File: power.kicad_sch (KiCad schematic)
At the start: 0 parts

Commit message: Fixed actuator channels to make GPIO expander sink instead of source current
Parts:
- added K?: J115F11C, actuation:J115F11C, symbol actuation:J115F11C
- added U?: TLI4971, Package_SON:Infineon_PG-TISON-8-5, symbol actuation:TLI4971
- added U?: ADS1110, Package_TO_SOT_SMD:SOT-23-6, symbol Analog_ADC:ADS1110
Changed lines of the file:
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@@
 (kicad_sch (version 20211123) (generator eeschema)
   (paper "A4")
+  (symbol (lib_id "actuation:J115F11C") (at 80.01 67.31 0) (unit 1)
+    (in_bom yes) (on_board yes) (fields_autoplaced)
+    (property "Reference" "K?" (id 0) (at 80.01 54.61 0))
+    (property "Value" "J115F11C" (id 1) (at 80.01 57.15 0))
+    (property "Footprint" "actuation:J115F11C" (id 2) (at 80.01 76.2 0)
+      (effects (font (size 1.27 1.27)) hide)
+    )
+    (property "Datasheet" "https://www.citrelay.com/Catalog%20Pages/RelayCatalog/J115F%2050amp.pdf" (id 3) (at 80.01 78.74 0)
+      (effects (font (size 1.27 1.27)) hide)
+    )
+    (property "MPN" "J115F11CH12VDCSH1.5U" (id 4) (at 80.01 81.28 0)
+      (effects (font (size 1.27 1.27)) hide)
+    )
+    (pin "1")
+    (pin "2")
+    (pin "3")
+    (pin "4")
+    (pin "5")
+  )
+  (symbol (lib_id "actuation:TLI4971") (at 124.46 90.17 0) (unit 1)
+    (in_bom yes) (on_board yes) (fields_autoplaced)
+    (property "Reference" "U?" (id 0) (at 124.46 85.09 0))
+    (property "Value" "TLI4971" (id 1) (at 124.46 87.63 0))
+    (property "Footprint" "Package_SON:Infineon_PG-TISON-8-5" (id 2) (at 124.46 109.22 0)
+      (effects (font (size 1.27 1.27)) hide)
+    )
+    (property "Datasheet" "https://www.infineon.com/dgdl/Infineon-TLI4971_25_50_75_120-DataSheet-v01_20-EN.pdf" (id 3) (at 124.46 111.76 0)
+      (effects (font (size 1.27 1.27)) hide)
+    )
+    (property "MPN" "TLI4971A050T5UE0001XUMA1" (id 4) (at 124.46 114.3 0)
+      (effects (font (size 1.27 1.27)) hide)
+    )
+    (pin "1")
+    (pin "2")
+    (pin "3")
+    (pin "4")
+    (pin "5")
+    (pin "6")
+    (pin "7")
+    (pin "8")
+  )
+  (symbol (lib_id "Analog_ADC:ADS1110") (at 179.07 69.85 0) (unit 1)
+    (in_bom yes) (on_board yes) (fields_autoplaced)
+    (property "Reference" "U?" (id 0) (at 181.0894 57.15 0)
+      (effects (font (size 1.27 1.27)) (justify left))
+    )
+    (property "Value" "ADS1110" (id 1) (at 181.0894 59.69 0)
+      (effects (font (size 1.27 1.27)) (justify left))
+    )
+    (property "Footprint" "Package_TO_SOT_SMD:SOT-23-6" (id 2) (at 190.5 60.96 0)
+      (effects (font (size 1.27 1.27)) (justify left) hide)
+    )
+    (property "Datasheet" "http://www.ti.com/lit/ds/symlink/ads1110.pdf" (id 3) (at 171.45 60.96 0)
+      (effects (font (size 1.27 1.27)) hide)
+    )
+    (pin "1")
+    (pin "2")
+    (pin "3")
+    (pin "4")
+    (pin "5")
+    (pin "6")
+  )
 )

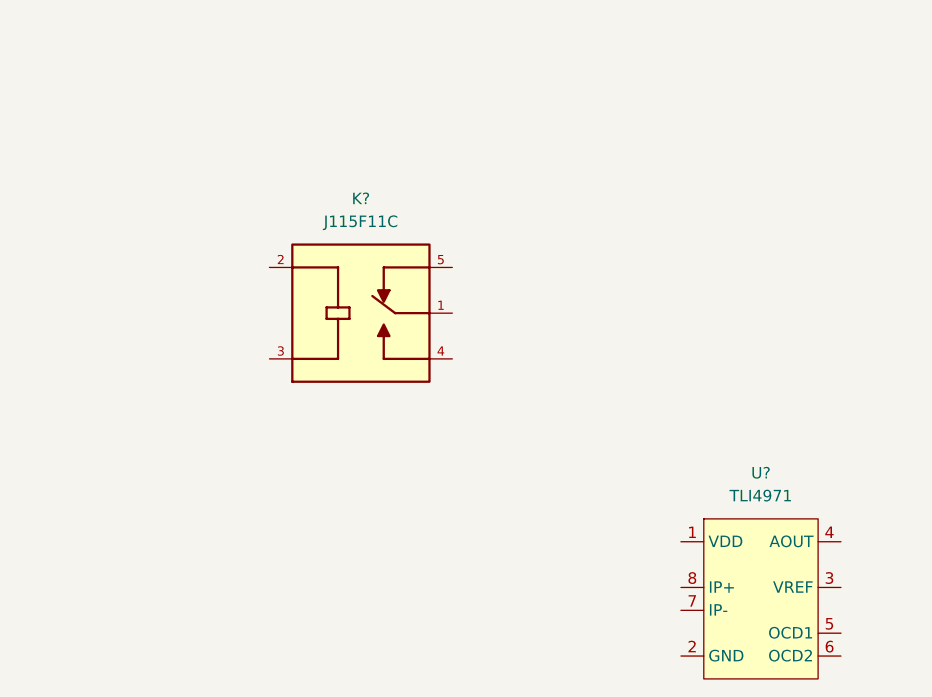
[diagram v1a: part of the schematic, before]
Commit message: Check-safe channel with buffer
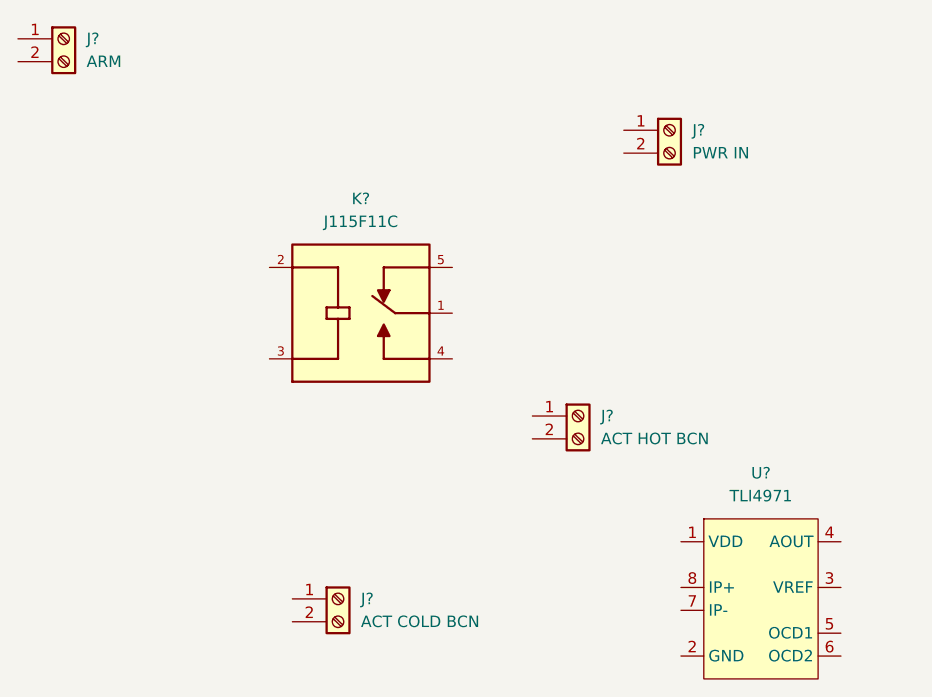
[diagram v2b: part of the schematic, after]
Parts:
- added J?: PWR IN, symbol Connector:Screw_Terminal_01x02
- added J?: ACT HOT BCN, symbol Connector:Screw_Terminal_01x02
- added J?: ACT COLD BCN, symbol Connector:Screw_Terminal_01x02
- added J?: ARM, symbol Connector:Screw_Terminal_01x02
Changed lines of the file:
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@@
     (pin "5")
+  )
+  (symbol (lib_id "Connector:Screw_Terminal_01x02") (at 114.3 46.99 0) (unit 1)
+    (in_bom yes) (on_board yes) (fields_autoplaced)
+    (property "Reference" "J?" (id 0) (at 116.84 46.9899 0)
+      (effects (font (size 1.27 1.27)) (justify left))
+    )
+    (property "Value" "PWR IN" (id 1) (at 116.84 49.5299 0)
+      (effects (font (size 1.27 1.27)) (justify left))
+    )
+    (property "Footprint" "" (id 2) (at 114.3 46.99 0)
+      (effects (font (size 1.27 1.27)) hide)
+    )
+    (property "Datasheet" "~" (id 3) (at 114.3 46.99 0)
+      (effects (font (size 1.27 1.27)) hide)
+    )
+    (pin "1")
+    (pin "2")
   )
   (symbol (lib_id "actuation:TLI4971") (at 124.46 90.17 0) (unit 1)
@@
     (pin "6")
   )
+  (symbol (lib_id "Connector:Screw_Terminal_01x02") (at 104.14 78.74 0) (unit 1)
+    (in_bom yes) (on_board yes) (fields_autoplaced)
+    (property "Reference" "J?" (id 0) (at 106.68 78.7399 0)
+      (effects (font (size 1.27 1.27)) (justify left))
+    )
+    (property "Value" "ACT HOT BCN" (id 1) (at 106.68 81.2799 0)
+      (effects (font (size 1.27 1.27)) (justify left))
+    )
+    (property "Footprint" "" (id 2) (at 104.14 78.74 0)
+      (effects (font (size 1.27 1.27)) hide)
+    )
+    (property "Datasheet" "~" (id 3) (at 104.14 78.74 0)
+      (effects (font (size 1.27 1.27)) hide)
+    )
+    (pin "1")
+    (pin "2")
+  )
+  (symbol (lib_id "Connector:Screw_Terminal_01x02") (at 77.47 99.06 0) (unit 1)
+    (in_bom yes) (on_board yes) (fields_autoplaced)
+    (property "Reference" "J?" (id 0) (at 80.01 99.0599 0)
+      (effects (font (size 1.27 1.27)) (justify left))
+    )
+    (property "Value" "ACT COLD BCN" (id 1) (at 80.01 101.5999 0)
+      (effects (font (size 1.27 1.27)) (justify left))
+    )
+    (property "Footprint" "" (id 2) (at 77.47 99.06 0)
+      (effects (font (size 1.27 1.27)) hide)
+    )
+    (property "Datasheet" "~" (id 3) (at 77.47 99.06 0)
+      (effects (font (size 1.27 1.27)) hide)
+    )
+    (pin "1")
+    (pin "2")
+  )
+  (symbol (lib_id "Connector:Screw_Terminal_01x02") (at 46.99 36.83 0) (unit 1)
+    (in_bom yes) (on_board yes) (fields_autoplaced)
+    (property "Reference" "J?" (id 0) (at 49.53 36.8299 0)
+      (effects (font (size 1.27 1.27)) (justify left))
+    )
+    (property "Value" "ARM" (id 1) (at 49.53 39.3699 0)
+      (effects (font (size 1.27 1.27)) (justify left))
+    )
+    (property "Footprint" "" (id 2) (at 46.99 36.83 0)
+      (effects (font (size 1.27 1.27)) hide)
+    )
+    (property "Datasheet" "~" (id 3) (at 46.99 36.83 0)
+      (effects (font (size 1.27 1.27)) hide)
+    )
+    (pin "1")
+    (pin "2")
+  )
 )

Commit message: Preliminary power scheme
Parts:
- J?: value ACT HOT BCN -> ACT HOT
- J?: value ACT COLD BCN -> ACT COLD
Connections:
- net VBUS: now reaches K?.1
- net VBUS: now also U?.7 (IP-)
- net at K?.2: now also J?.2 (Pin_2)
- net at K?.3: now also J?.1 (Pin_1)
- net Vdrive: now reaches K?.4
- net Vdrive: now also J?.1 (Pin_1)
- net VSAFE: now reaches K?.5
- net VSAFE: now also J?.1 (Pin_1)
- net at J?.1 (Pin_1): now also U?.8 (IP+)
- net GNDPWR: now reaches J?.2 (Pin_2)
- net GNDPWR: now also J?.2 (Pin_2), J?.2 (Pin_2)
- net +3.3V: now reaches U?.1 (VDD)
- net +3.3V: now also U?.5 (VDD)
- net GND: now reaches U?.2 (GND)
- net GND: now also U?.2 (GND)
- net at U?.3 (VREF): now also U?.6 (VIN-)
- net at U?.4 (AOUT): now also U?.1 (VIN+)
- net SCL: now reaches U?.3 (SCL)
- net SDA: now reaches U?.4 (SDA)
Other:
- moved on the sheet: J?, K?, U?

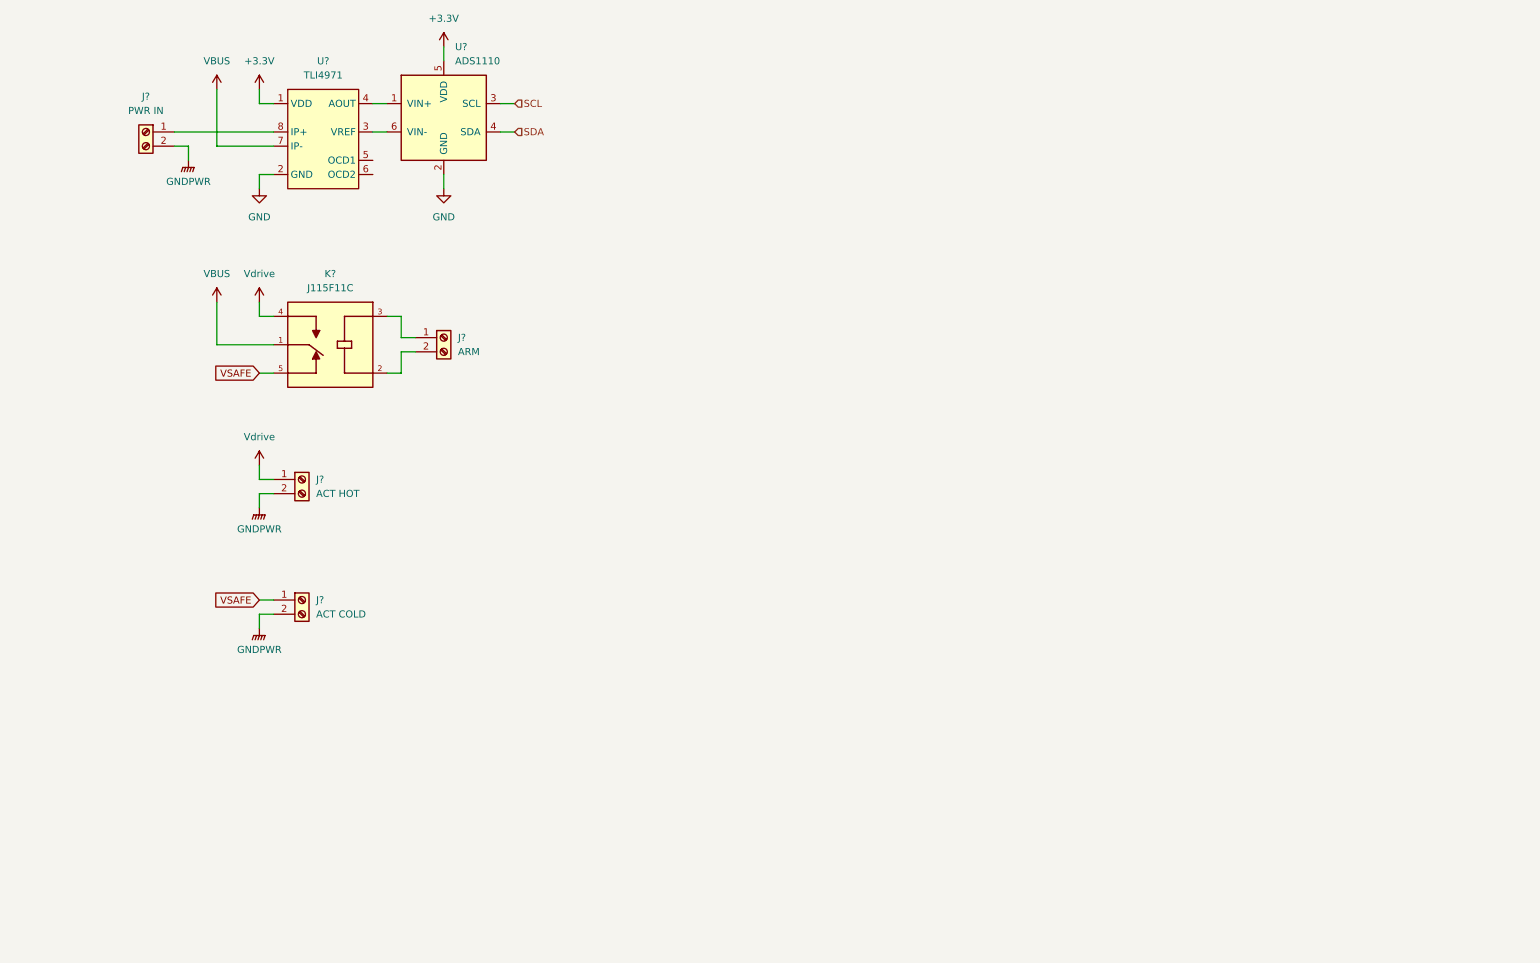
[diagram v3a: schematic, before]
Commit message: ADC filtering and decoupling for current sense
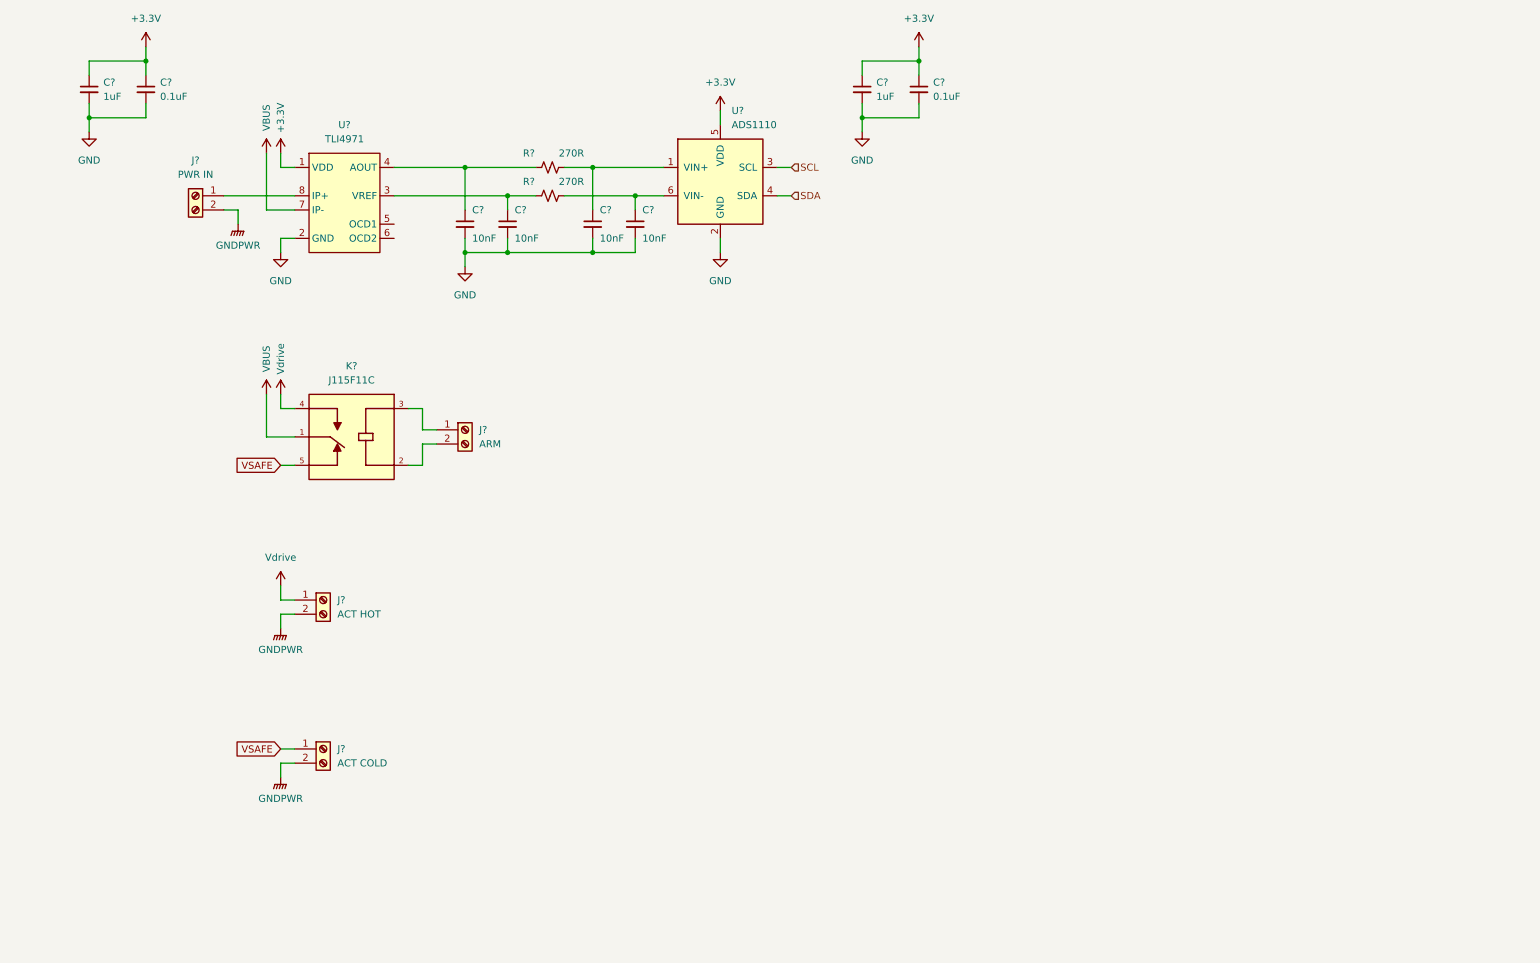
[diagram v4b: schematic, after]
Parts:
- added C? (x4): 10nF, symbol Device:C_Small
- added C? (x2): 1uF, Capacitor_SMD:C_0603_1608Metric, symbol Device:C_Small
- added C? (x2): 0.1uF, Capacitor_SMD:C_0603_1608Metric, symbol Device:C_Small
- added R? (x2): 270R, symbol Device:R_Small_US
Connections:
- net +3.3V: now also C?.1, C?.1, C?.1, C?.1
- net GND: now also C?.2, C?.2, C?.2, C?.2, C?.2, C?.2, C?.2, C?.2
- net at U?.3 (VREF): now also C?.1, R?.1; no longer U?.6 (VIN-)
- net at U?.1 (VIN+): now also C?.1, R?.2; no longer U?.4 (AOUT)
- new net: C?.1, R?.1, U?.4 (AOUT)
- new net: C?.1, R?.2, U?.6 (VIN-)
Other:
- moved on the sheet: J?, K?, U?

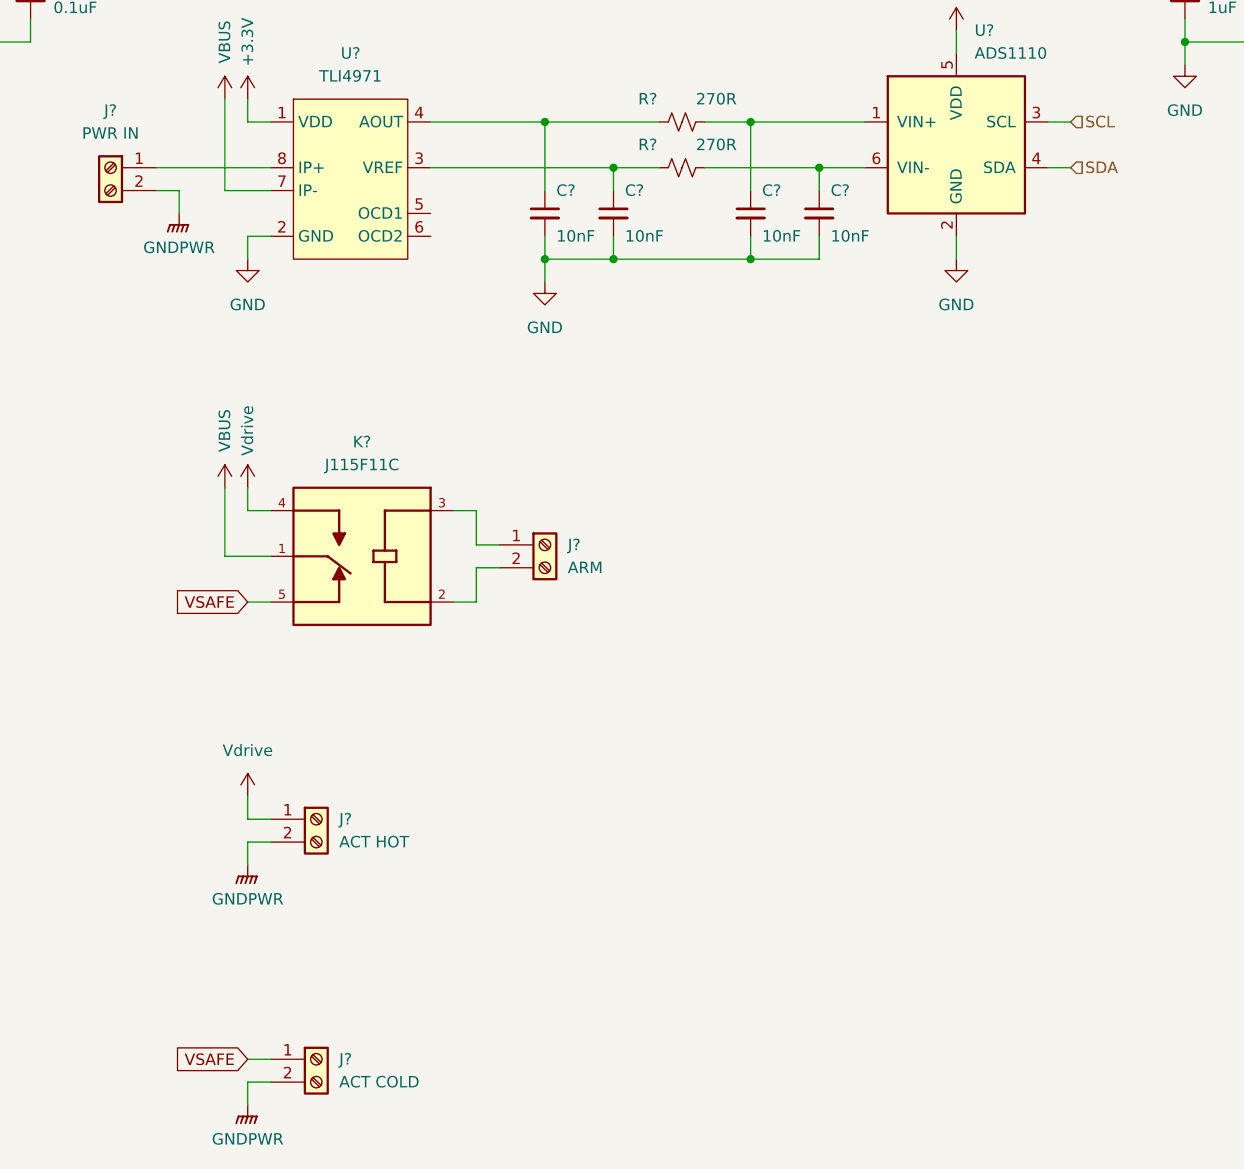
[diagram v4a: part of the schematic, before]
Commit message: Created arming circuit controllable by C&C
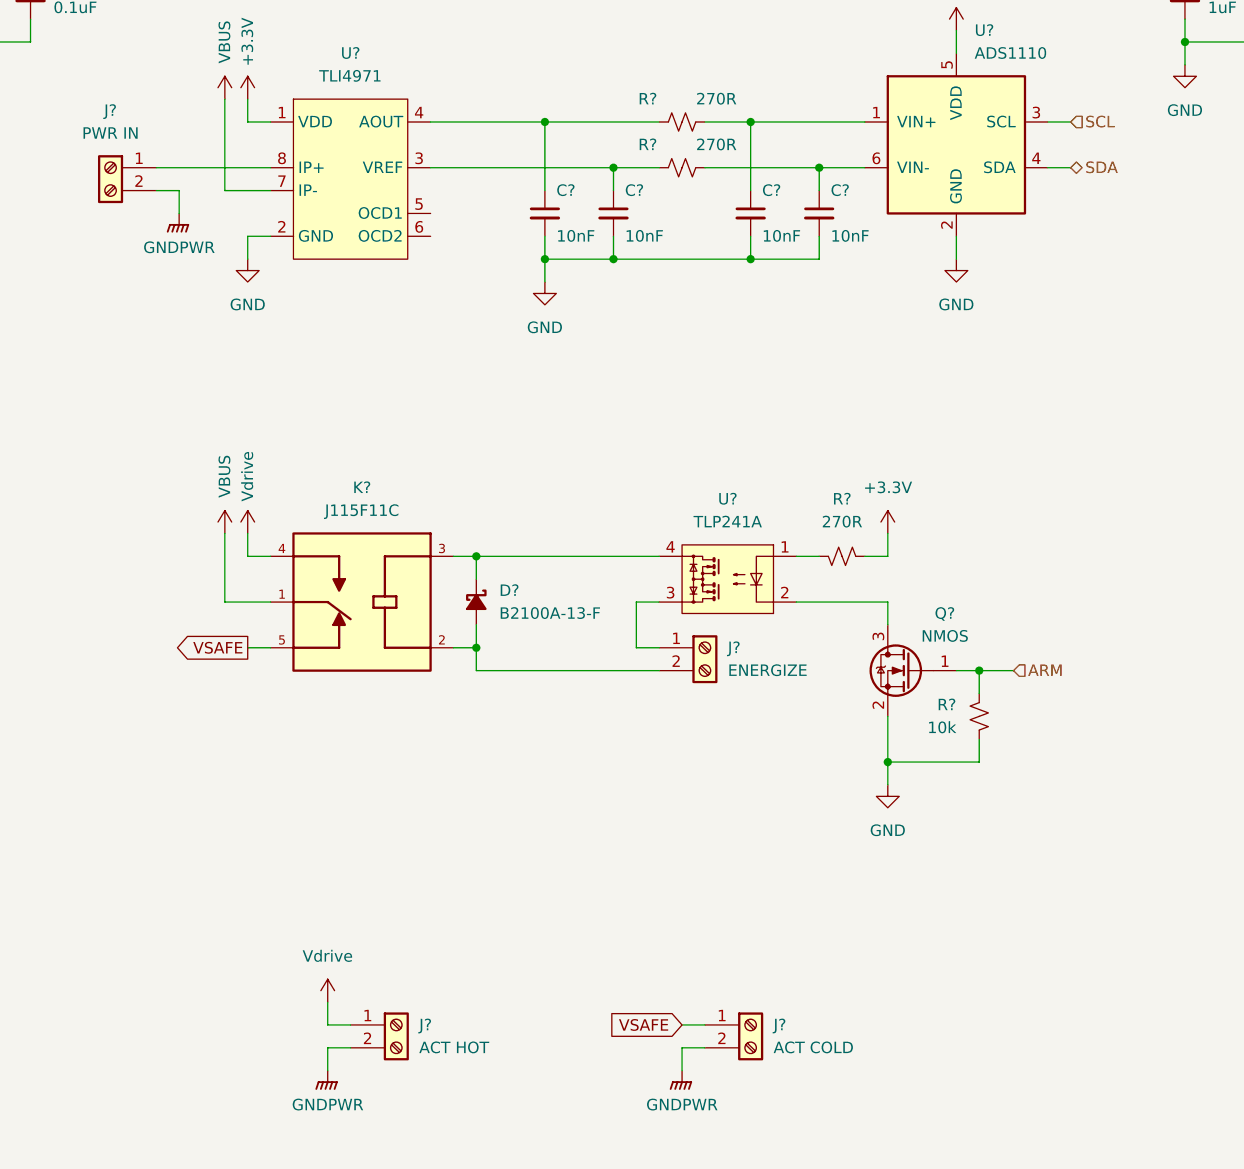
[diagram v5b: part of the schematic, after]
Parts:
- added D?: B2100A-13-F, Diode_SMD:D_SMA, symbol Device:D_Schottky_Small_Filled
- added Q?: NMOS, symbol Device:Q_NMOS_GSD
- added R?: 10k, symbol Device:R_Small_US
- added R?: 270R, Resistor_SMD:R_0603_1608Metric, symbol Device:R_Small_US
- added U?: TLP241A, actuation:11-5B2S, symbol actuation:TLP241A
- J?: value ARM -> ENERGIZE
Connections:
- net +3.3V: now also R?.1
- net GND: now also Q?.2 (S), R?.2
- net at J?.2 (Pin_2), K?.2: now also D?.2 (A)
- net at K?.3: now also D?.1 (K), U?.4; no longer J?.1 (Pin_1)
- new net: J?.1 (Pin_1), U?.3
- new net: R?.2, U?.1
- new net: Q?.3 (D), U?.2
- new net ARM: Q?.1 (G), R?.1
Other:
- moved on the sheet: J?, K?
